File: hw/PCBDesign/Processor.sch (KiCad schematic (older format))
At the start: 2 parts

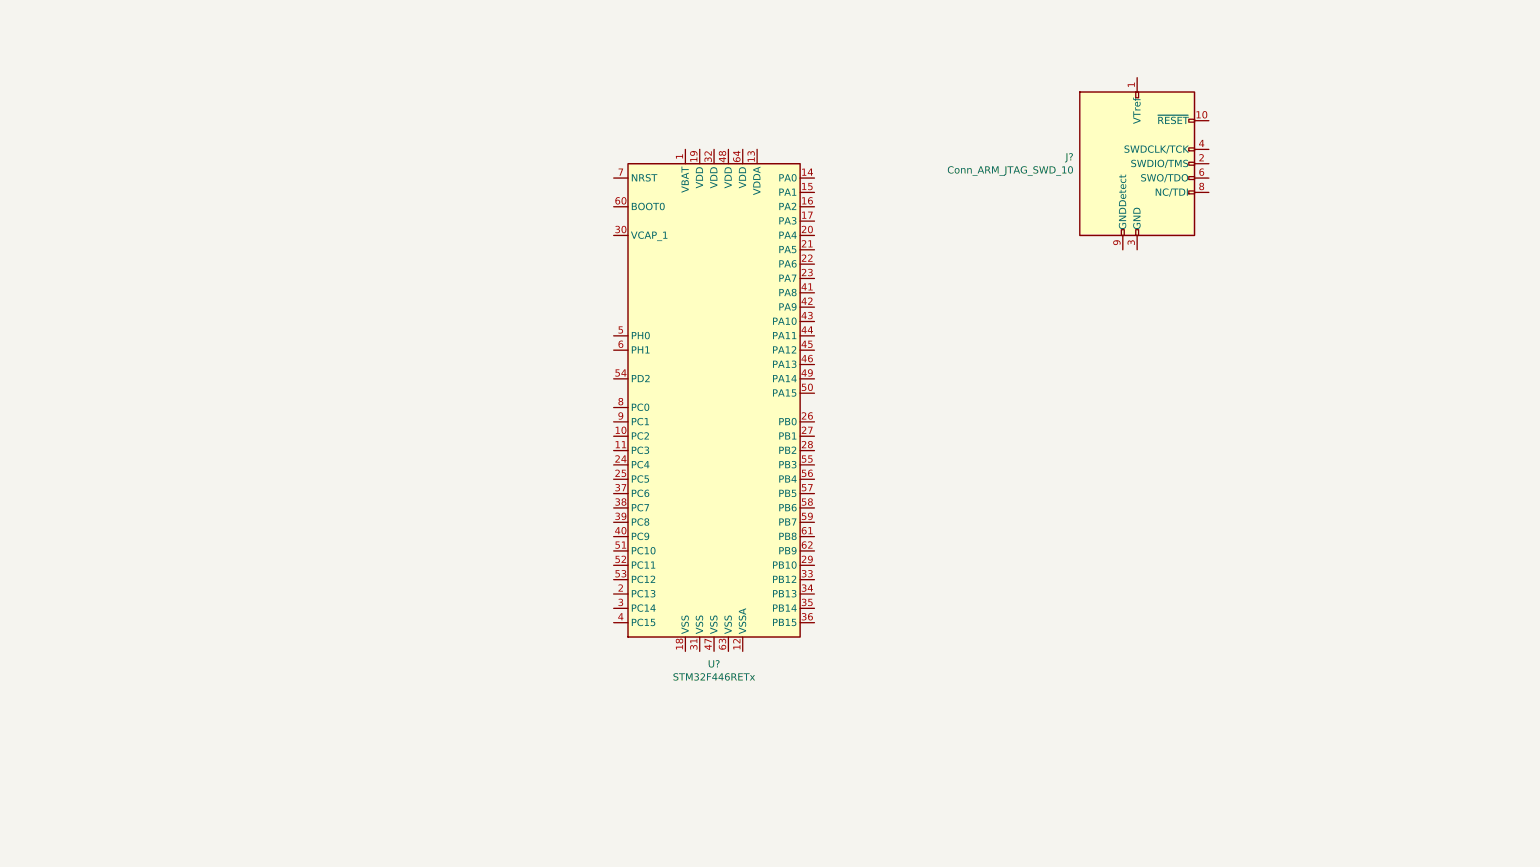
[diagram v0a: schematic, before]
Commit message: Fill out a lot of the board schematic
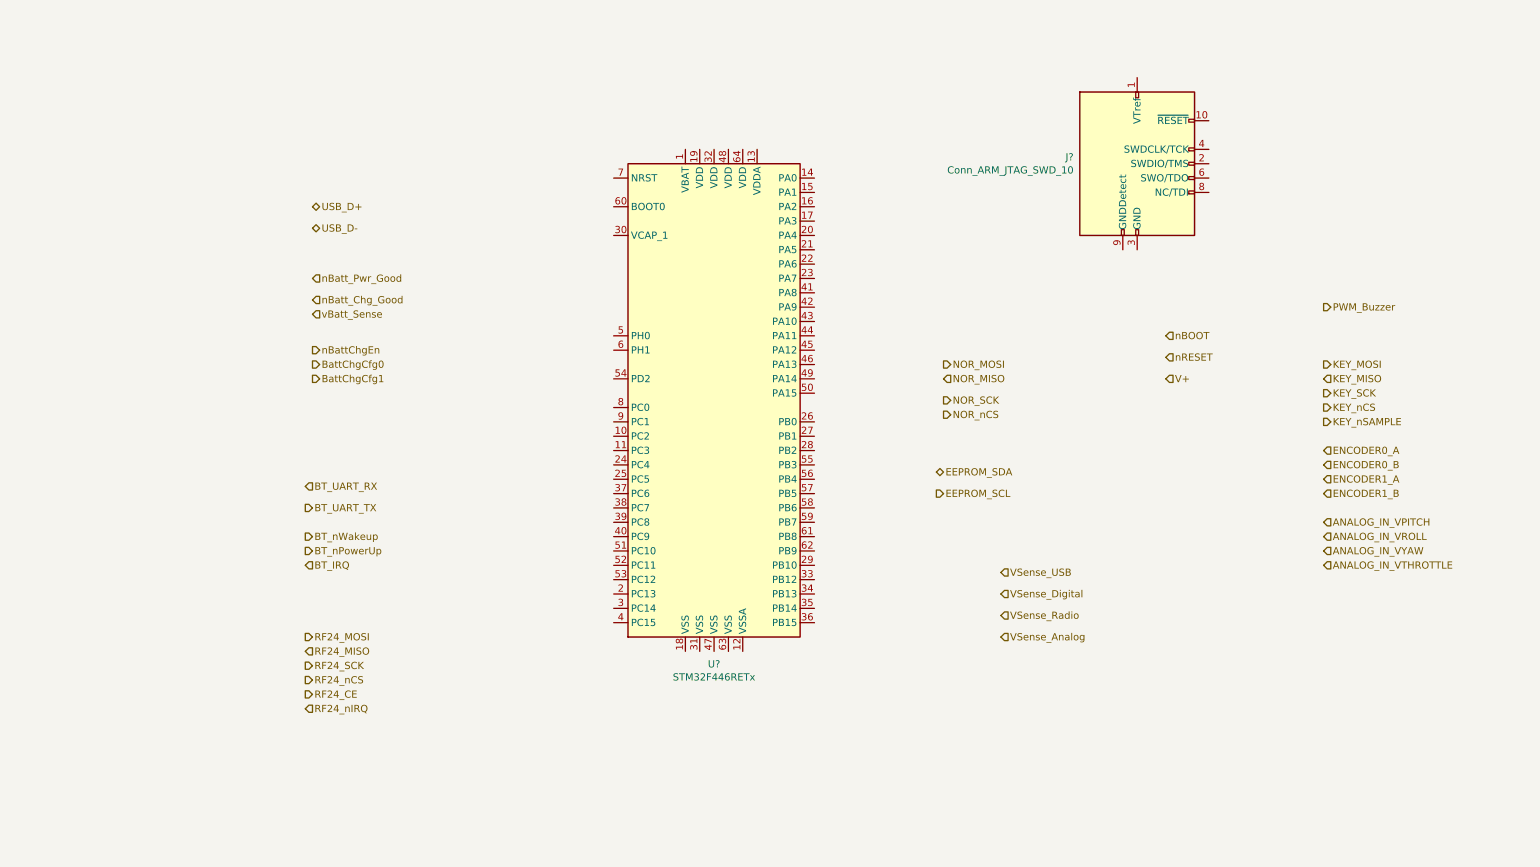
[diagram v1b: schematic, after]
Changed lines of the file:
@@
 $Descr A4 11693 8268
 encoding utf-8
-Sheet 4 5
+Sheet 11 11
 Title ""
 Date ""
@@
 	1    0    0    -1
 $EndComp
+Text HLabel 2650 2050 2    50   BiDi ~ 0
+USB_D+
+Text HLabel 2650 2200 2    50   BiDi ~ 0
+USB_D-
+Text HLabel 2650 2550 2    50   Input ~ 0
+nBatt_Pwr_Good
+Text HLabel 2650 2700 2    50   Input ~ 0
+nBatt_Chg_Good
+Text HLabel 2650 2800 2    50   Input ~ 0
+vBatt_Sense
+Text HLabel 2650 3050 2    50   Output ~ 0
+nBattChgEn
+Text HLabel 2650 3150 2    50   Output ~ 0
+BattChgCfg0
+Text HLabel 2650 3250 2    50   Output ~ 0
+BattChgCfg1
+Text HLabel 2600 4000 2    50   Input ~ 0
+BT_UART_RX
+Text HLabel 2600 4150 2    50   Output ~ 0
+BT_UART_TX
+Text HLabel 2600 4350 2    50   Output ~ 0
+BT_nWakeup
+Text HLabel 2600 4450 2    50   Output ~ 0
+BT_nPowerUp
+Text HLabel 2600 4550 2    50   Input ~ 0
+BT_IRQ
+Text HLabel 2600 5050 2    50   Output ~ 0
+RF24_MOSI
+Text HLabel 2600 5150 2    50   Input ~ 0
+RF24_MISO
+Text HLabel 2600 5250 2    50   Output ~ 0
+RF24_SCK
+Text HLabel 2600 5350 2    50   Output ~ 0
+RF24_nCS
+Text HLabel 2600 5450 2    50   Output ~ 0
+RF24_CE
+Text HLabel 2600 5550 2    50   Input ~ 0
+RF24_nIRQ
+Text HLabel 7050 3150 2    50   Output ~ 0
+NOR_MOSI
+Text HLabel 7050 3250 2    50   Input ~ 0
+NOR_MISO
+Text HLabel 7050 3400 2    50   Output ~ 0
+NOR_SCK
+Text HLabel 7050 3500 2    50   Output ~ 0
+NOR_nCS
+Text HLabel 7000 3900 2    50   BiDi ~ 0
+EEPROM_SDA
+Text HLabel 7000 4050 2    50   Output ~ 0
+EEPROM_SCL
+Text HLabel 7450 4600 2    50   Input ~ 0
+VSense_USB
+Text HLabel 7450 4750 2    50   Input ~ 0
+VSense_Digital
+Text HLabel 7450 4900 2    50   Input ~ 0
+VSense_Radio
+Text HLabel 7450 5050 2    50   Input ~ 0
+VSense_Analog
+Text HLabel 8600 3250 2    50   Input ~ 0
+V+
+Text HLabel 8600 3100 2    50   Input ~ 0
+nRESET
+Text HLabel 8600 2950 2    50   Input ~ 0
+nBOOT
+Text HLabel 9700 2750 2    50   Output ~ 0
+PWM_Buzzer
+Text HLabel 9700 3150 2    50   Output ~ 0
+KEY_MOSI
+Text HLabel 9700 3250 2    50   Input ~ 0
+KEY_MISO
+Text HLabel 9700 3350 2    50   Output ~ 0
+KEY_SCK
+Text HLabel 9700 3450 2    50   Output ~ 0
+KEY_nCS
+Text HLabel 9700 3550 2    50   Output ~ 0
+KEY_nSAMPLE
+Text HLabel 9700 3750 2    50   Input ~ 0
+ENCODER0_A
+Text HLabel 9700 3850 2    50   Input ~ 0
+ENCODER0_B
+Text HLabel 9700 3950 2    50   Input ~ 0
+ENCODER1_A
+Text HLabel 9700 4050 2    50   Input ~ 0
+ENCODER1_B
+Text HLabel 9700 4250 2    50   Input ~ 0
+ANALOG_IN_VPITCH
+Text HLabel 9700 4350 2    50   Input ~ 0
+ANALOG_IN_VROLL
+Text HLabel 9700 4450 2    50   Input ~ 0
+ANALOG_IN_VYAW
+Text HLabel 9700 4550 2    50   Input ~ 0
+ANALOG_IN_VTHROTTLE
 $EndSCHEMATC

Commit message: Routed JTAG and power to the processor
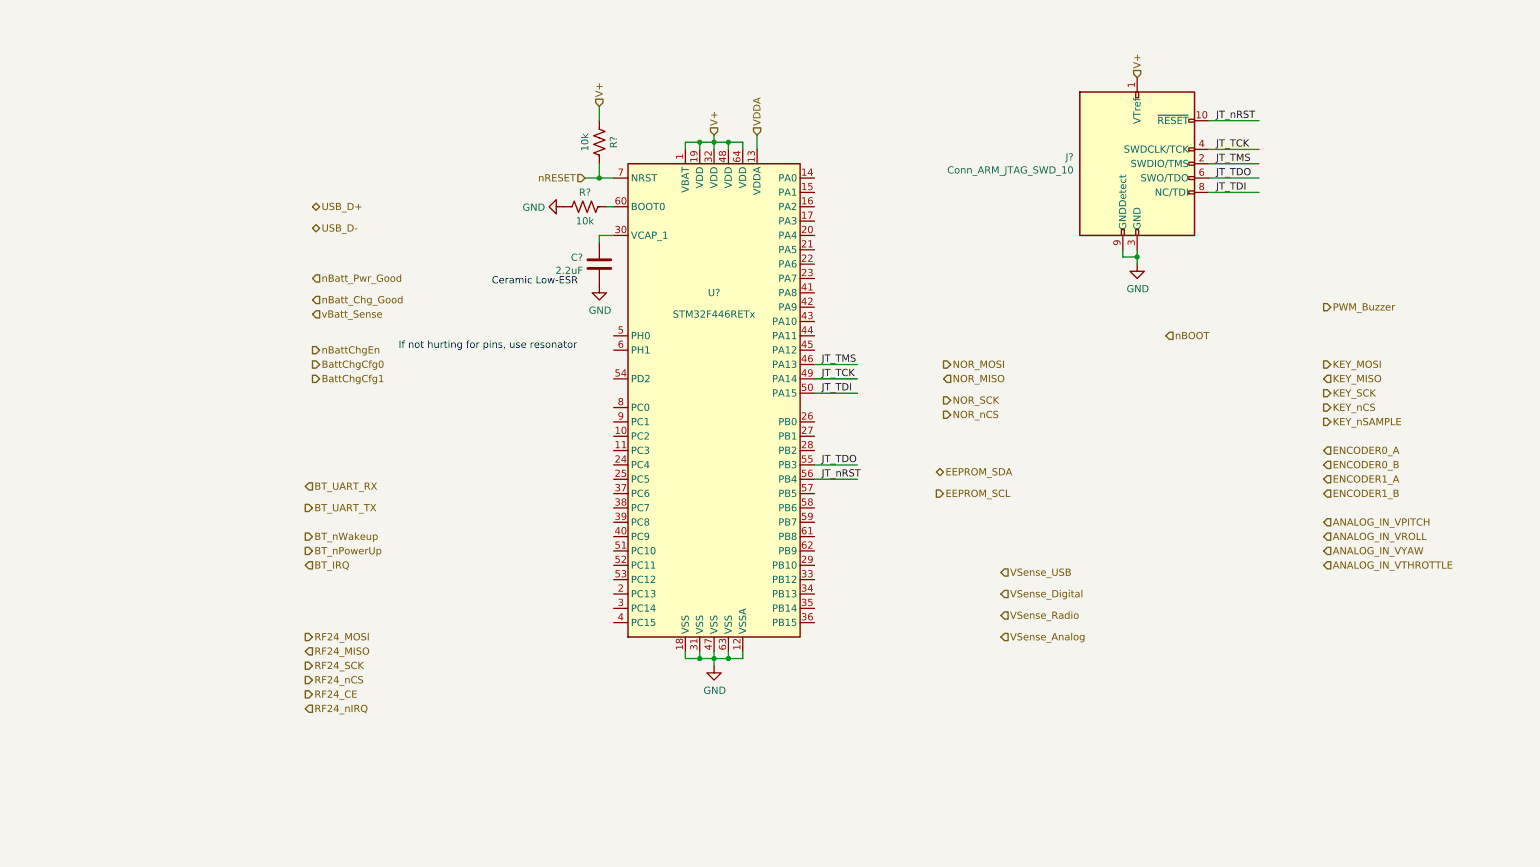
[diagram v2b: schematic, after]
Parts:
- added C?: 2.2uF, symbol Device:C
- added R? (x2): 10k, symbol Device:R_US
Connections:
- net labels added: GND, JT_TCK, JT_TDI, JT_TDO, JT_TMS, JT_nRST, VDDA
- wire segments 0 -> 42
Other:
- note added: "Ceramic Low-ESR"
- note added: "If not hurting for pins, use resonator"
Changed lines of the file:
@@
 U 1 1 6047114C
 P 5450 3350
-F 0 "U?" H 5450 1461 50  0000 C CNN
-F 1 "STM32F446RETx" H 5450 1370 50  0000 C CNN
+F 0 "U?" H 5450 4050 50  0000 C CNN
+F 1 "STM32F446RETx" H 5450 3900 50  0000 C CNN
 F 2 "Package_QFP:LQFP-64_10x10mm_P0.5mm" H 4850 1650 50  0001 R CNN
 F 3 "http://www.st.com/st-web-ui/static/active/en/resource/technical/document/datasheet/DM00141306.pdf" H 5450 3350 50  0001 C CNN
@@
 Text HLabel 7450 5050 2    50   Input ~ 0
 VSense_Analog
-Text HLabel 8600 3250 2    50   Input ~ 0
+Text HLabel 5450 1550 1    50   Input ~ 0
 V+
-Text HLabel 8600 3100 2    50   Input ~ 0
+Text HLabel 4550 1850 0    50   Input ~ 0
 nRESET
 Text HLabel 8600 2950 2    50   Input ~ 0
@@
 Text HLabel 9700 4550 2    50   Input ~ 0
 ANALOG_IN_VTHROTTLE
+Wire Wire Line
+	8900 1450 9250 1450
+Wire Wire Line
+	8900 1650 9250 1650
+Wire Wire Line
+	8900 1750 9250 1750
+Wire Wire Line
+	8900 1850 9250 1850
+Wire Wire Line
+	8900 1950 9250 1950
+Text HLabel 8400 1150 1    50   Input ~ 0
+V+
+$Comp
+L power:GND #PWR?
+U 1 1 605AD389
+P 8400 2450
+F 0 "#PWR?" H 8400 2200 50  0001 C CNN
+F 1 "GND" H 8405 2277 50  0000 C CNN
+F 2 "" H 8400 2450 50  0001 C CNN
+F 3 "" H 8400 2450 50  0001 C CNN
+	1    8400 2450
+	1    0    0    -1
+$EndComp
+Wire Wire Line
+	8400 2350 8400 2400
+Wire Wire Line
+	8300 2350 8300 2400
+Wire Wire Line
+	8300 2400 8400 2400
+Connection ~ 8400 2400
+Wire Wire Line
+	8400 2400 8400 2450
+$Comp
+L power:GND #PWR?
+U 1 1 605ADCEE
+P 5450 5250
+F 0 "#PWR?" H 5450 5000 50  0001 C CNN
+F 1 "GND" H 5455 5077 50  0000 C CNN
+F 2 "" H 5450 5250 50  0001 C CNN
+F 3 "" H 5450 5250 50  0001 C CNN
+	1    5450 5250
+	1    0    0    -1
+$EndComp
+Wire Wire Line
+	5450 5150 5450 5200
+Wire Wire Line
+	5450 5200 5550 5200
+Wire Wire Line
+	5550 5200 5550 5150
+Connection ~ 5450 5200
+Wire Wire Line
+	5450 5200 5450 5250
+Wire Wire Line
+	5550 5200 5650 5200
+Wire Wire Line
+	5650 5200 5650 5150
+Connection ~ 5550 5200
+Wire Wire Line
+	5450 5200 5350 5200
+Wire Wire Line
+	5350 5200 5350 5150
+Wire Wire Line
+	5350 5200 5250 5200
+Wire Wire Line
+	5250 5200 5250 5150
+Connection ~ 5350 5200
+Text Label 8950 1450 0    50   ~ 0
+JT_nRST
+Text Label 8950 1650 0    50   ~ 0
+JT_TCK
+Text Label 8950 1750 0    50   ~ 0
+JT_TMS
+Text Label 8950 1850 0    50   ~ 0
+JT_TDO
+Text Label 8950 1950 0    50   ~ 0
+JT_TDI
+Text Label 6200 3950 0    50   ~ 0
+JT_nRST
+Wire Wire Line
+	5450 1550 5450 1600
+Wire Wire Line
+	5550 1650 5550 1600
+Wire Wire Line
+	5550 1600 5450 1600
+Connection ~ 5450 1600
+Wire Wire Line
+	5450 1600 5450 1650
+Wire Wire Line
+	5650 1650 5650 1600
+Wire Wire Line
+	5650 1600 5550 1600
+Connection ~ 5550 1600
+Wire Wire Line
+	5350 1650 5350 1600
+Wire Wire Line
+	5350 1600 5450 1600
+Wire Wire Line
+	5250 1650 5250 1600
+Wire Wire Line
+	5250 1600 5350 1600
+Connection ~ 5350 1600
+Text HLabel 5750 1550 1    50   Input ~ 0
+VDDA
+Wire Wire Line
+	5750 1550 5750 1650
+$Comp
+L Device:R_US R?
+U 1 1 605B24E0
+P 4550 2050
+F 0 "R?" V 4450 2050 50  0000 C CNN
+F 1 "10k" V 4650 2050 50  0000 C CNN
+F 2 "" V 4590 2040 50  0001 C CNN
+F 3 "~" H 4550 2050 50  0001 C CNN
+	1    4550 2050
+	0    1    1    0
+$EndComp
+Wire Wire Line
+	4700 2050 4750 2050
+$Comp
+L power:GND #PWR?
+U 1 1 605B3866
+P 4400 2050
+F 0 "#PWR?" H 4400 1800 50  0001 C CNN
+F 1 "GND" V 4405 1922 50  0000 R CNN
+F 2 "" H 4400 2050 50  0001 C CNN
+F 3 "" H 4400 2050 50  0001 C CNN
+	1    4400 2050
+	0    1    1    0
+$EndComp
+$Comp
+L Device:C C?
+U 1 1 605B4044
+P 4650 2450
+F 0 "C?" H 4536 2404 50  0000 R CNN
+F 1 "2.2uF" H 4536 2495 50  0000 R CNN
+F 2 "" H 4688 2300 50  0001 C CNN
+F 3 "~" H 4650 2450 50  0001 C CNN
+	1    4650 2450
+	1    0    0    1
+$EndComp
+$Comp
+L power:GND #PWR?
+U 1 1 605B4752
+P 4650 2600
+F 0 "#PWR?" H 4650 2350 50  0001 C CNN
+F 1 "GND" H 4655 2427 50  0000 C CNN
+F 2 "" H 4650 2600 50  0001 C CNN
+F 3 "" H 4650 2600 50  0001 C CNN
+	1    4650 2600
+	1    0    0    -1
+$EndComp
+Wire Wire Line
+	4650 2300 4650 2250
+Wire Wire Line
+	4650 2250 4750 2250
+Text Notes 3900 2600 0    50   ~ 0
+Ceramic Low-ESR
+$Comp
+L Device:R_US R?
+U 1 1 605B572A
+P 4650 1600
+F 0 "R?" V 4550 1600 50  0000 C CNN
+F 1 "10k" V 4750 1600 50  0000 C CNN
+F 2 "" V 4690 1590 50  0001 C CNN
+F 3 "~" H 4650 1600 50  0001 C CNN
+	1    4650 1600
+	-1   0    0    1
+$EndComp
+Wire Wire Line
+	4650 1750 4650 1850
+Text HLabel 4650 1350 1    50   Input ~ 0
+V+
+Wire Wire Line
+	4650 1350 4650 1450
+Wire Wire Line
+	6150 3850 6450 3850
+Text Label 6200 3850 0    50   ~ 0
+JT_TDO
+Wire Wire Line
+	6150 3950 6450 3950
+Wire Wire Line
+	4650 1850 4750 1850
+Wire Wire Line
+	4550 1850 4650 1850
+Connection ~ 4650 1850
+Wire Wire Line
+	6150 3350 6450 3350
+Text Label 6200 3350 0    50   ~ 0
+JT_TDI
+Wire Wire Line
+	6150 3250 6450 3250
+Text Label 6200 3250 0    50   ~ 0
+JT_TCK
+Wire Wire Line
+	6150 3150 6450 3150
+Text Label 6200 3150 0    50   ~ 0
+JT_TMS
+Text Notes 3250 3050 0    50   ~ 0
+If not hurting for pins, use resonator
 $EndSCHEMATC

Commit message: Planned out some of the system level connections on the processor IO
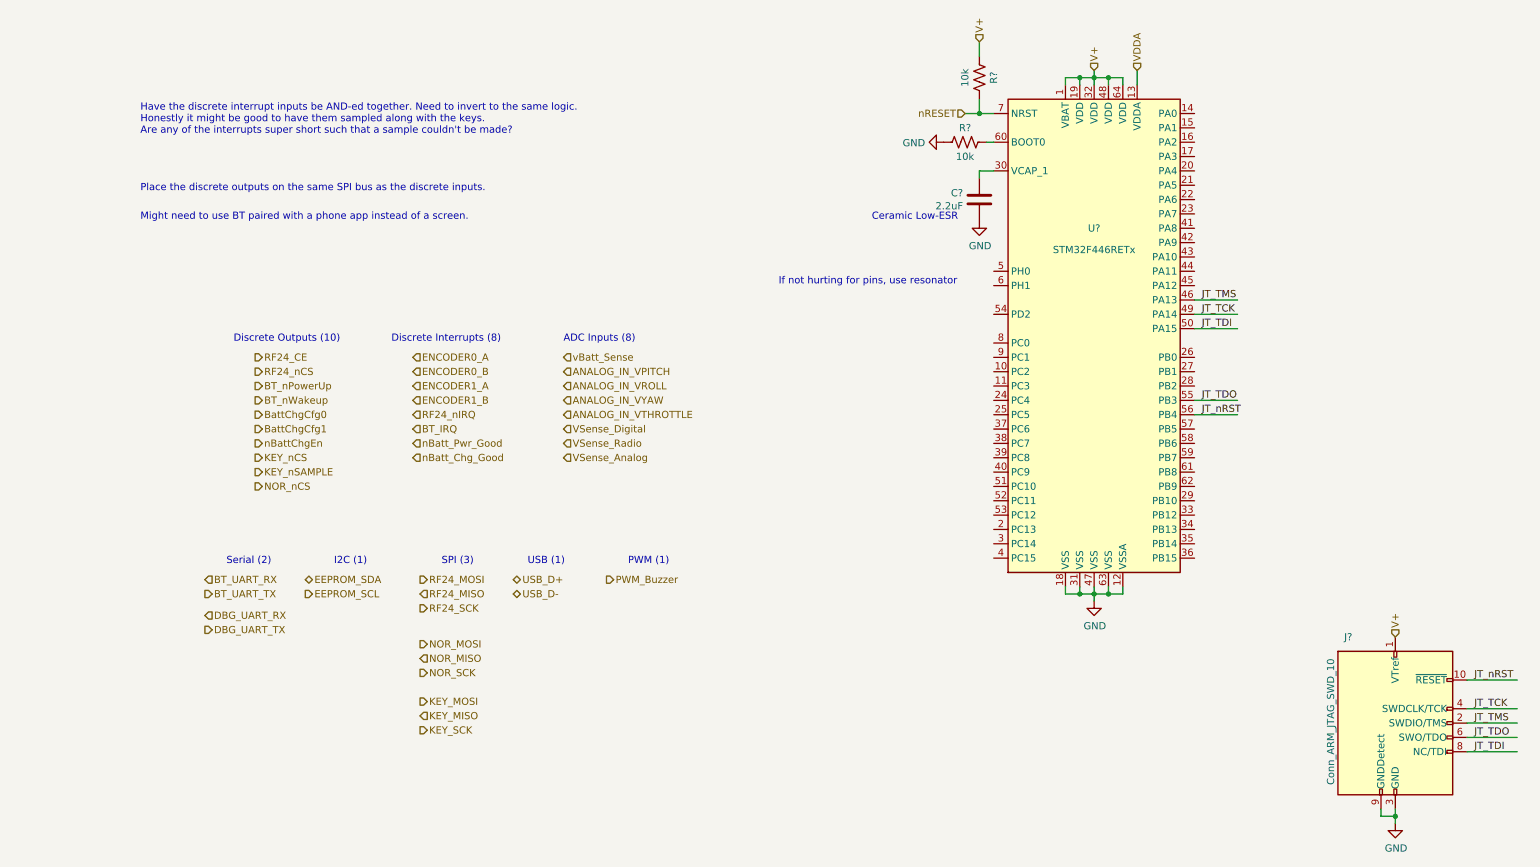
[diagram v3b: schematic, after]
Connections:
- net labels added: DBG_UART_RX, DBG_UART_TX
- net labels removed: VSense_USB, nBOOT
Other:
- note added: "ADC Inputs (8)"
- note added: "Discrete Interrupts (8)"
- note added: "Discrete Outputs (10)"
- note added: "Have the discrete interrupt inputs be AND-ed together. Need to invert to the same logic.\nHonestly it might be good to have them sampled along with the keys.\nAre any of the interrupts super short such that a sample couldn't be made?"
- note added: "I2C (1)"
- note added: "Might need to use BT paired with a phone app instead of a screen."
- note added: "PWM (1)"
- note added: "Place the discrete outputs on the same SPI bus as the discrete inputs."
- note added: "SPI (3)"
- note added: "Serial (2)"
- note added: "USB (1)"
- moved on the sheet: C?, J?, R?, U?
